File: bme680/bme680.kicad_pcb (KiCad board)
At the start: 4 copper layers, 7 parts, among them U1 BME680

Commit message: [Rushil] added default id on skillscreen
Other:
- board text added: "Addr 0x77"
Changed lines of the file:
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@@
 		(layer "Dwgs.User")
+	)
+	(gr_text "Addr\n0x77"
+		(at 117.5 72.25 0)
+		(layer "F.SilkS")
+		(effects
+			(font
+				(size 0.6 0.6)
+				(thickness 0.15)
+				(bold yes)
+			)
+			(justify left bottom)
+		)
 	)
 	(gr_text "BME680"

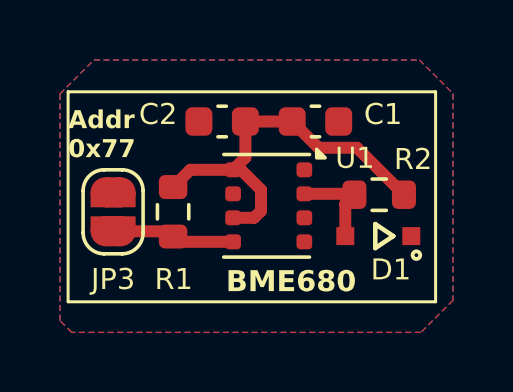
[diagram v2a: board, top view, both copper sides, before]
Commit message: [Rushil] corrected pcb added information on both schematic and pcb user drawing correct circuit of bno055
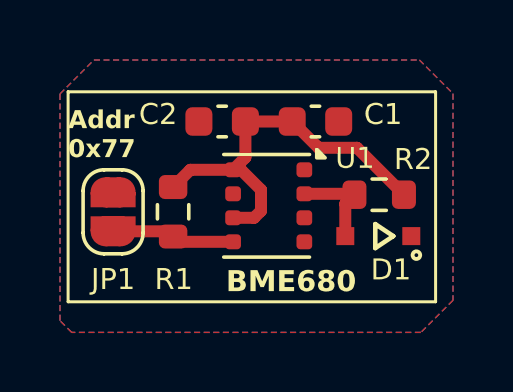
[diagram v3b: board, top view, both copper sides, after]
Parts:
- renumbered JP3 to JP1
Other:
- board text added: "Avoid ground planes and high-current traces beneath or near the sensor to prevent heat buildup"
- board text added: "Environmental sensor for temperature, humidity, pressure, and gas (VOC)."
- board text added: "KEEP OUT AREA LAYER 2 AND 3 sensor area"
- board text removed: "KEEP OUT AREA LAYER 2 AND 3"
- board text removed: "avoid ground plane just below sensor and avoid high current trace near by sensor and under it which can heat it up."
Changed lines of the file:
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@@
 		(descr "SMD Solder Jumper, 1x1.5mm, rounded Pads, 0.3mm gap, open")
 		(tags "solder jumper open")
-		(property "Reference" "JP3"
+		(property "Reference" "JP1"
 			(at 2.25 0 180)
 			(layer "F.SilkS")
@@
 		)
 	)
-	(gr_text "avoid ground plane just below sensor\nand avoid high current trace near by\nsensor and under it which can heat \nit up."
-		(at 117.5 72.45 0)
+	(gr_text "Environmental sensor for temperature, \nhumidity, pressure, and gas (VOC)."
+		(at 117.74 76.85 0)
 		(layer "Dwgs.User")
 		(effects
@@
 		)
 	)
-	(gr_text "KEEP OUT \nAREA\nLAYER 2 \nAND 3"
-		(at 122.61 75.07 0)
+	(gr_text "Avoid ground planes and high-current\ntraces beneath or near the sensor \nto prevent heat buildup"
+		(at 117.59 71.82 0)
 		(layer "Dwgs.User")
 		(effects
@@
 				(size 0.4 0.4)
 				(thickness 0.1)
+				(bold yes)
 			)
 			(justify left bottom)
 		)
 	)
-	(gr_text "BME680"
-		(at 122.75 76.71 0)
+	(gr_text "KEEP OUT \nAREA\nLAYER 2 \nAND 3\nsensor area"
+		(at 122.27 75.27 0)
 		(layer "Dwgs.User")
 		(effects
 			(font
-				(size 0.7 0.7)
-				(thickness 0.153)
+				(size 0.4 0.4)
+				(thickness 0.1)
+			)
+			(justify left bottom)
+		)
+	)
+	(gr_text "BME680"
+		(at 128 75.25 90)
+		(layer "Dwgs.User")
+		(effects
+			(font
+				(size 0.5 0.5)
+				(thickness 0.125)
 				(bold yes)
 			)

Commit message: bug fixes in BME680
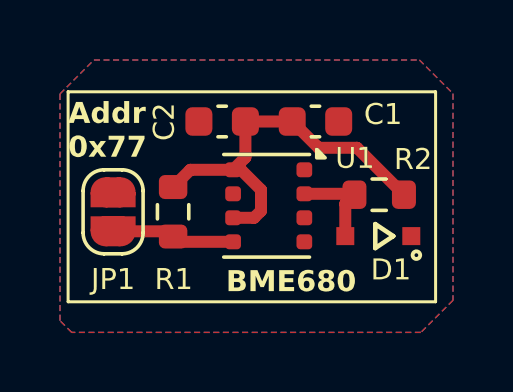
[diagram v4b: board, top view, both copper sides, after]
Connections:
- net /block_bme680/+3V3 renamed /BME680/+3V3
- net /block_bme680/CS renamed /BME680/CS
- net /block_bme680/GND renamed /BME680/GND
- net /block_bme680/SCK renamed /BME680/SCK
- net /block_bme680/SD0/ADDR renamed /BME680/SD0/ADDR
- net /block_bme680/SDI renamed /BME680/SDI
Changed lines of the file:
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@@
 			(psa4output no)
 			(plot_black_and_white yes)
+			(plotinvisibletext no)
 			(sketchpadsonfab no)
 			(plotpadnumbers no)
@@
 	)
 	(net 0 "")
-	(net 1 "/block_bme680/CS")
-	(net 2 "/block_bme680/GND")
-	(net 3 "/block_bme680/SD0{slash}ADDR")
-	(net 4 "/block_bme680/+3V3")
-	(net 5 "/block_bme680/SCK")
-	(net 6 "/block_bme680/SDI")
+	(net 1 "/BME680/+3V3")
+	(net 2 "/BME680/GND")
+	(net 3 "/BME680/CS")
+	(net 4 "/BME680/SD0{slash}ADDR")
+	(net 5 "/BME680/SCK")
+	(net 6 "/BME680/SDI")
 	(net 7 "Net-(U1-CSB)")
 	(footprint "Library:Bosch_LGA-8_3x3mm_P0.8mm_ClockwisePinNumbering"
@@
 		)
 		(property ki_fp_filters "*LGA*3x3mm*P0.8mm*Clockwise*")
-		(sheetname "/block_bme680/")
+		(sheetname "/BME680/")
 		(sheetfile "block_bme680.kicad_sch")
 		(attr smd)
@@
 			(layers "F.Cu" "F.Mask" "F.Paste")
 			(roundrect_rratio 0.25)
-			(net 2 "/block_bme680/GND")
+			(net 2 "/BME680/GND")
 			(pinfunction "GND")
 			(pintype "power_in")
@@
 			(layers "F.Cu" "F.Mask" "F.Paste")
 			(roundrect_rratio 0.25)
-			(net 6 "/block_bme680/SDI")
+			(net 6 "/BME680/SDI")
 			(pinfunction "SDI")
 			(pintype "bidirectional")
@@
 			(layers "F.Cu" "F.Mask" "F.Paste")
 			(roundrect_rratio 0.25)
-			(net 5 "/block_bme680/SCK")
+			(net 5 "/BME680/SCK")
 			(pinfunction "SCK")
 			(pintype "input")
@@
 			(layers "F.Cu" "F.Mask" "F.Paste")
 			(roundrect_rratio 0.25)
-			(net 3 "/block_bme680/SD0{slash}ADDR")
+			(net 4 "/BME680/SD0{slash}ADDR")
 			(pinfunction "SDO")
 			(pintype "bidirectional")
@@
 			(layers "F.Cu" "F.Mask" "F.Paste")
 			(roundrect_rratio 0.25)
-			(net 4 "/block_bme680/+3V3")
+			(net 1 "/BME680/+3V3")
 			(pinfunction "VDDIO")
 			(pintype "power_in")
@@
 			(layers "F.Cu" "F.Mask" "F.Paste")
 			(roundrect_rratio 0.25)
-			(net 2 "/block_bme680/GND")
+			(net 2 "/BME680/GND")
 			(pinfunction "GND")
 			(pintype "power_in")
@@
 			(layers "F.Cu" "F.Mask" "F.Paste")
 			(roundrect_rratio 0.25)
-			(net 4 "/block_bme680/+3V3")
+			(net 1 "/BME680/+3V3")
 			(pinfunction "VDD")
 			(pintype "power_in")
@@
 			)
 		)
-		(sheetname "/block_bme680/")
+		(sheetname "/BME680/")
 		(sheetfile "block_bme680.kicad_sch")
 		(attr smd)
@@
 			(size 0.6 0.6)
 			(layers "F.Cu" "F.Mask" "F.Paste")
-			(net 1 "/block_bme680/CS")
+			(net 3 "/BME680/CS")
 			(pintype "passive")
 			(solder_mask_margin 0.102)
@@
 		)
 		(property ki_fp_filters "R_*")
-		(sheetname "/block_bme680/")
+		(sheetname "/BME680/")
 		(sheetfile "block_bme680.kicad_sch")
 		(attr smd)
@@
 			(layers "F.Cu" "F.Mask" "F.Paste")
 			(roundrect_rratio 0.25)
-			(net 4 "/block_bme680/+3V3")
+			(net 1 "/BME680/+3V3")
 			(pintype "passive")
 		)
@@
 		)
 		(property ki_fp_filters "R_*")
-		(sheetname "/block_bme680/")
+		(sheetname "/BME680/")
 		(sheetfile "block_bme680.kicad_sch")
 		(attr smd)
@@
 			(layers "F.Cu" "F.Mask" "F.Paste")
 			(roundrect_rratio 0.25)
-			(net 4 "/block_bme680/+3V3")
+			(net 1 "/BME680/+3V3")
 			(pintype "passive")
 		)
@@
 			(layers "F.Cu" "F.Mask" "F.Paste")
 			(roundrect_rratio 0.25)
-			(net 3 "/block_bme680/SD0{slash}ADDR")
+			(net 4 "/BME680/SD0{slash}ADDR")
 			(pintype "passive")
 		)
@@
 		(tags "capacitor")
 		(property "Reference" "C2"
-			(at 2.135 0.24 0)
+			(at 1.935 -0.01 90)
 			(layer "F.SilkS")
 			(effects
@@
 		)
 		(property ki_fp_filters "C_*")
-		(sheetname "/block_bme680/")
+		(sheetname "/BME680/")
 		(sheetfile "block_bme680.kicad_sch")
 		(attr smd)
@@
 			(layers "F.Cu" "F.Mask" "F.Paste")
 			(roundrect_rratio 0.25)
-			(net 4 "/block_bme680/+3V3")
+			(net 1 "/BME680/+3V3")
 			(pintype "passive")
 		)
@@
 			(layers "F.Cu" "F.Mask" "F.Paste")
 			(roundrect_rratio 0.25)
-			(net 2 "/block_bme680/GND")
+			(net 2 "/BME680/GND")
 			(pintype "passive")
 		)
@@
 		)
 		(property ki_fp_filters "Jumper* TestPoint*2Pads* TestPoint*Bridge*")
-		(sheetname "/block_bme680/")
+		(sheetname "/BME680/")
 		(sheetfile "block_bme680.kicad_sch")
 		(zone_connect 1)
@@
 			(size 1 0.5)
 			(layers "F.Cu" "F.Mask")
-			(net 2 "/block_bme680/GND")
+			(net 2 "/BME680/GND")
 			(pinfunction "A")
 			(pintype "passive")
@@
 			(size 1 0.5)
 			(layers "F.Cu" "F.Mask")
-			(net 3 "/block_bme680/SD0{slash}ADDR")
+			(net 4 "/BME680/SD0{slash}ADDR")
 			(pinfunction "B")
 			(pintype "passive")
@@
 		)
 		(property ki_fp_filters "C_*")
-		(sheetname "/block_bme680/")
+		(sheetname "/BME680/")
 		(sheetfile "block_bme680.kicad_sch")
 		(attr smd)
@@
 			(layers "F.Cu" "F.Mask" "F.Paste")
 			(roundrect_rratio 0.25)
-			(net 4 "/block_bme680/+3V3")
+			(net 1 "/BME680/+3V3")
 			(pintype "passive")
 		)
@@
 			(layers "F.Cu" "F.Mask" "F.Paste")
 			(roundrect_rratio 0.25)
-			(net 2 "/block_bme680/GND")
+			(net 2 "/BME680/GND")
 			(pintype "passive")
 		)
@@
 		(effects
 			(font
-				(size 0.6 0.6)
-				(thickness 0.15)
+				(size 0.7 0.7)
+				(thickness 0.1531)
 				(bold yes)
 			)
@@
 	)
 	(segment
+		(start 123 74.2)
+		(end 123.7 74.2)
+		(width 0.4)
+		(layer "F.Cu")
+		(net 1)
+	)
+	(segment
+		(start 123.41 70.99)
+		(end 123.41 72.19)
+		(width 0.4)
+		(layer "F.Cu")
+		(net 1)
+	)
+	(segment
+		(start 123.41 70.99)
+		(end 124.97 70.99)
+		(width 0.4)
+		(layer "F.Cu")
+		(net 1)
+	)
+	(segment
+		(start 123.41 72.19)
+		(end 123 72.6)
+		(width 0.4)
+		(layer "F.Cu")
+		(net 1)
+	)
+	(segment
+		(start 123.262499 72.6)
+		(end 123 72.6)
+		(width 0.4)
+		(layer "F.Cu")
+		(net 1)
+	)
+	(segment
+		(start 124.97 70.99)
+		(end 125.846 71.866)
+		(width 0.4)
+		(layer "F.Cu")
+		(net 1)
+	)
+	(segment
+		(start 125.846 71.866)
+		(end 127.131 71.866)
+		(width 0.4)
+		(layer "F.Cu")
+		(net 1)
+	)
+	(segment
+		(start 121 73.175)
+		(end 121.575 72.6)
+		(width 0.4)
+		(layer "F.Cu")
+		(net 1)
+	)
+	(segment
+		(start 123.93 73.267501)
+		(end 123.262499 72.6)
+		(width 0.4)
+		(layer "F.Cu")
+		(net 1)
+	)
+	(segment
+		(start 123.93 73.97)
+		(end 123.93 73.267501)
+		(width 0.4)
+		(layer "F.Cu")
+		(net 1)
+	)
+	(segment
+		(start 127.131 71.866)
+		(end 128.695 73.43)
+		(width 0.4)
+		(layer "F.Cu")
+		(net 1)
+	)
+	(segment
+		(start 123.7 74.2)
+		(end 123.93 73.97)
+		(width 0.4)
+		(layer "F.Cu")
+		(net 1)
+	)
+	(segment
+		(start 121.575 72.6)
+		(end 123 72.6)
+		(width 0.4)
+		(layer "F.Cu")
+		(net 1)
+	)
+	(segment
 		(start 120.825 74.65)
 		(end 121 74.825)
 		(width 0.4)
 		(layer "F.Cu")
-		(net 3)
+		(net 4)
 	)
 	(segment
@@
 		(width 0.4)
 		(layer "F.Cu")
-		(net 3)
+		(net 4)
 	)
 	(segment
@@
 		(width 0.4)
 		(layer "F.Cu")
-		(net 3)
+		(net 4)
 	)
 	(segment
@@
 		(width 0.4)
 		(layer "F.Cu")
-		(net 3)
-	)
-	(segment
-		(start 123 74.2)
-		(end 123.7 74.2)
-		(width 0.4)
-		(layer "F.Cu")
-		(net 4)
-	)
-	(segment
-		(start 123.41 70.99)
-		(end 123.41 72.19)
-		(width 0.4)
-		(layer "F.Cu")
-		(net 4)
-	)
-	(segment
-		(start 123.41 70.99)
-		(end 124.97 70.99)
-		(width 0.4)
-		(layer "F.Cu")
-		(net 4)
-	)
-	(segment
-		(start 123.41 72.19)
-		(end 123 72.6)
-		(width 0.4)
-		(layer "F.Cu")
-		(net 4)
-	)
-	(segment
-		(start 123.262499 72.6)
-		(end 123 72.6)
-		(width 0.4)
-		(layer "F.Cu")
-		(net 4)
-	)
-	(segment
-		(start 124.97 70.99)
-		(end 125.846 71.866)
-		(width 0.4)
-		(layer "F.Cu")
-		(net 4)
-	)
-	(segment
-		(start 125.846 71.866)
-		(end 127.131 71.866)
-		(width 0.4)
-		(layer "F.Cu")
-		(net 4)
-	)
-	(segment
-		(start 121 73.175)
-		(end 121.575 72.6)
-		(width 0.4)
-		(layer "F.Cu")
-		(net 4)
-	)
-	(segment
-		(start 123.93 73.267501)
-		(end 123.262499 72.6)
-		(width 0.4)
-		(layer "F.Cu")
-		(net 4)
-	)
-	(segment
-		(start 123.93 73.97)
-		(end 123.93 73.267501)
-		(width 0.4)
-		(layer "F.Cu")
-		(net 4)
-	)
-	(segment
-		(start 127.131 71.866)
-		(end 128.695 73.43)
-		(width 0.4)
-		(layer "F.Cu")
-		(net 4)
-	)
-	(segment
-		(start 123.7 74.2)
-		(end 123.93 73.97)
-		(width 0.4)
-		(layer "F.Cu")
-		(net 4)
-	)
-	(segment
-		(start 121.575 72.6)
-		(end 123 72.6)
-		(width 0.4)
-		(layer "F.Cu")
 		(net 4)
 	)
@@
 	(zone
 		(net 2)
-		(net_name "/block_bme680/GND")
+		(net_name "/BME680/GND")
 		(layers "F.Cu" "B.Cu" "In1.Cu" "In2.Cu")
 		(name "TBR")
